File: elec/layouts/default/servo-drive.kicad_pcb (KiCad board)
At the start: 4 copper layers, 46 x 42.3 mm, 105 parts

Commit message: lots of dumb little mistaktes
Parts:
- C1, C10, C11, C12, C14, C15, C16, C18, C19, C2, C3, C33, C34, C4, C41, C43, C45, C46, C47, C5, C6, C7, C8, C9: footprint Capacitor_SMD:C_0603_1608Metric -> Capacitor_SMD:C_0402_1005Metric
- R1, R10, R11, R14, R15, R17, R18, R19, R2, R20, R21, R22, R27, R28, R3, R32, R33, R34, R35, R36, R37, R38, R39, R40, R41, R42, R43, R44, R45, R46, R7, R9: footprint Resistor_SMD:R_0603_1608Metric -> Resistor_SMD:R_0402_1005Metric
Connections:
- net servo_drive.ato:ServoDrive.power_stage.half_bridge_a.hs_fet.gate renamed servo_drive.ato:ServoDrive.power_stage.half_bridge_a.fets.gate_top
- net servo_drive.ato:ServoDrive.power_stage.half_bridge_a.ls_fet.gate renamed servo_drive.ato:ServoDrive.power_stage.half_bridge_a.fets.gate_bottom
- net servo_drive.ato:ServoDrive.power_stage.half_bridge_b.hs_fet.gate renamed servo_drive.ato:ServoDrive.power_stage.half_bridge_b.fets.gate_top
- net servo_drive.ato:ServoDrive.power_stage.half_bridge_b.ls_fet.gate renamed servo_drive.ato:ServoDrive.power_stage.half_bridge_b.fets.gate_bottom
- net servo_drive.ato:ServoDrive.power_stage.half_bridge_c.hs_fet.gate renamed servo_drive.ato:ServoDrive.power_stage.half_bridge_c.fets.gate_top
- net servo_drive.ato:ServoDrive.power_stage.half_bridge_c.ls_fet.gate renamed servo_drive.ato:ServoDrive.power_stage.half_bridge_c.fets.gate_bottom

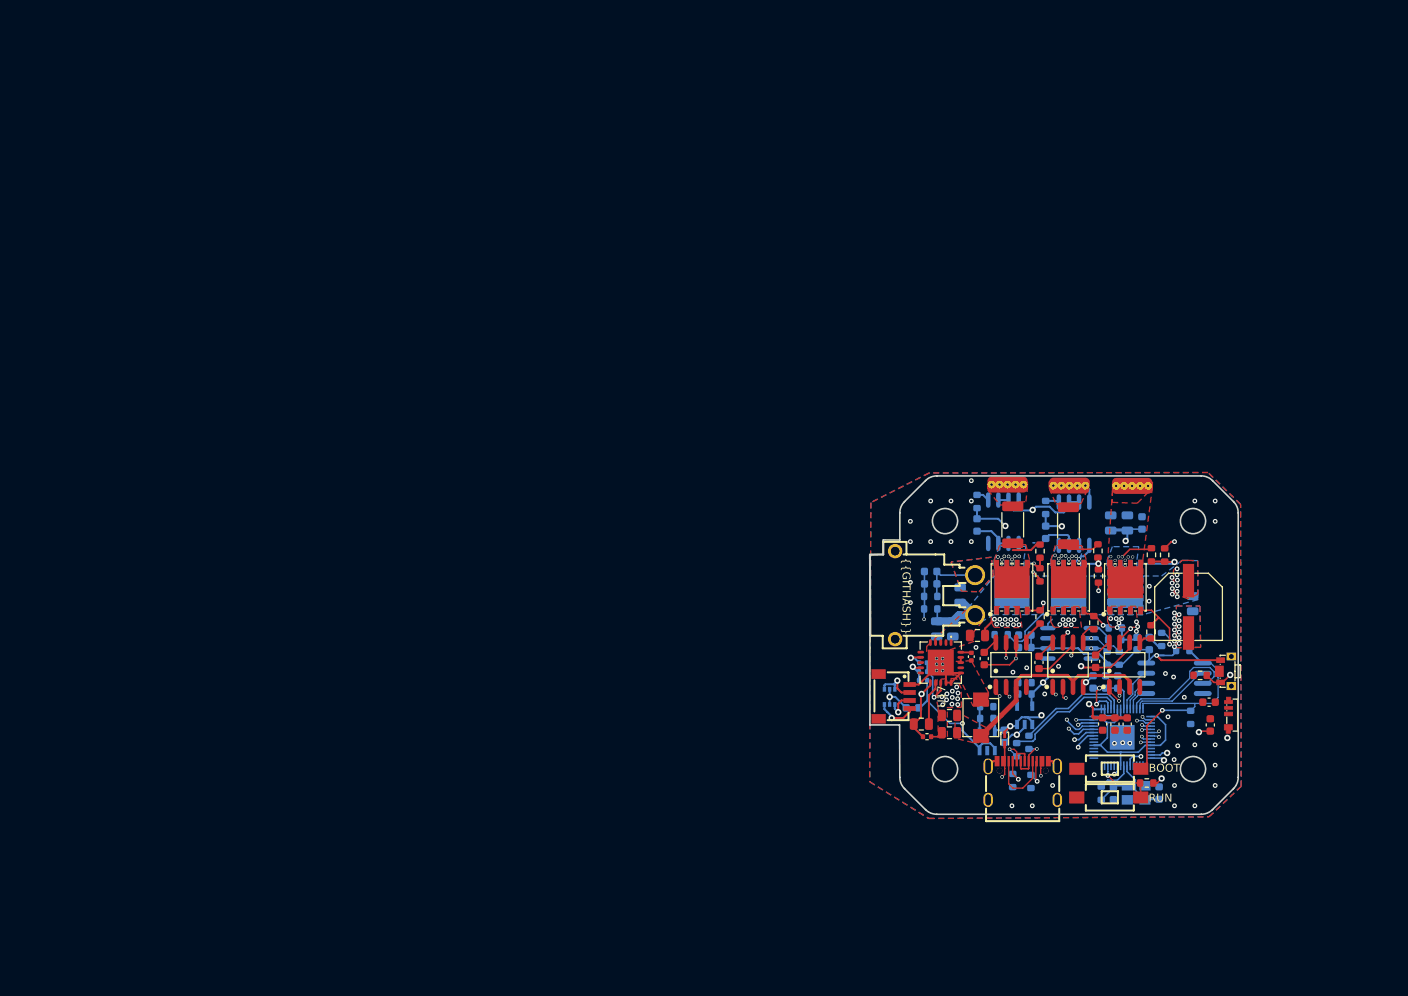
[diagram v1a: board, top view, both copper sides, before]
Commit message: mechanical outline change
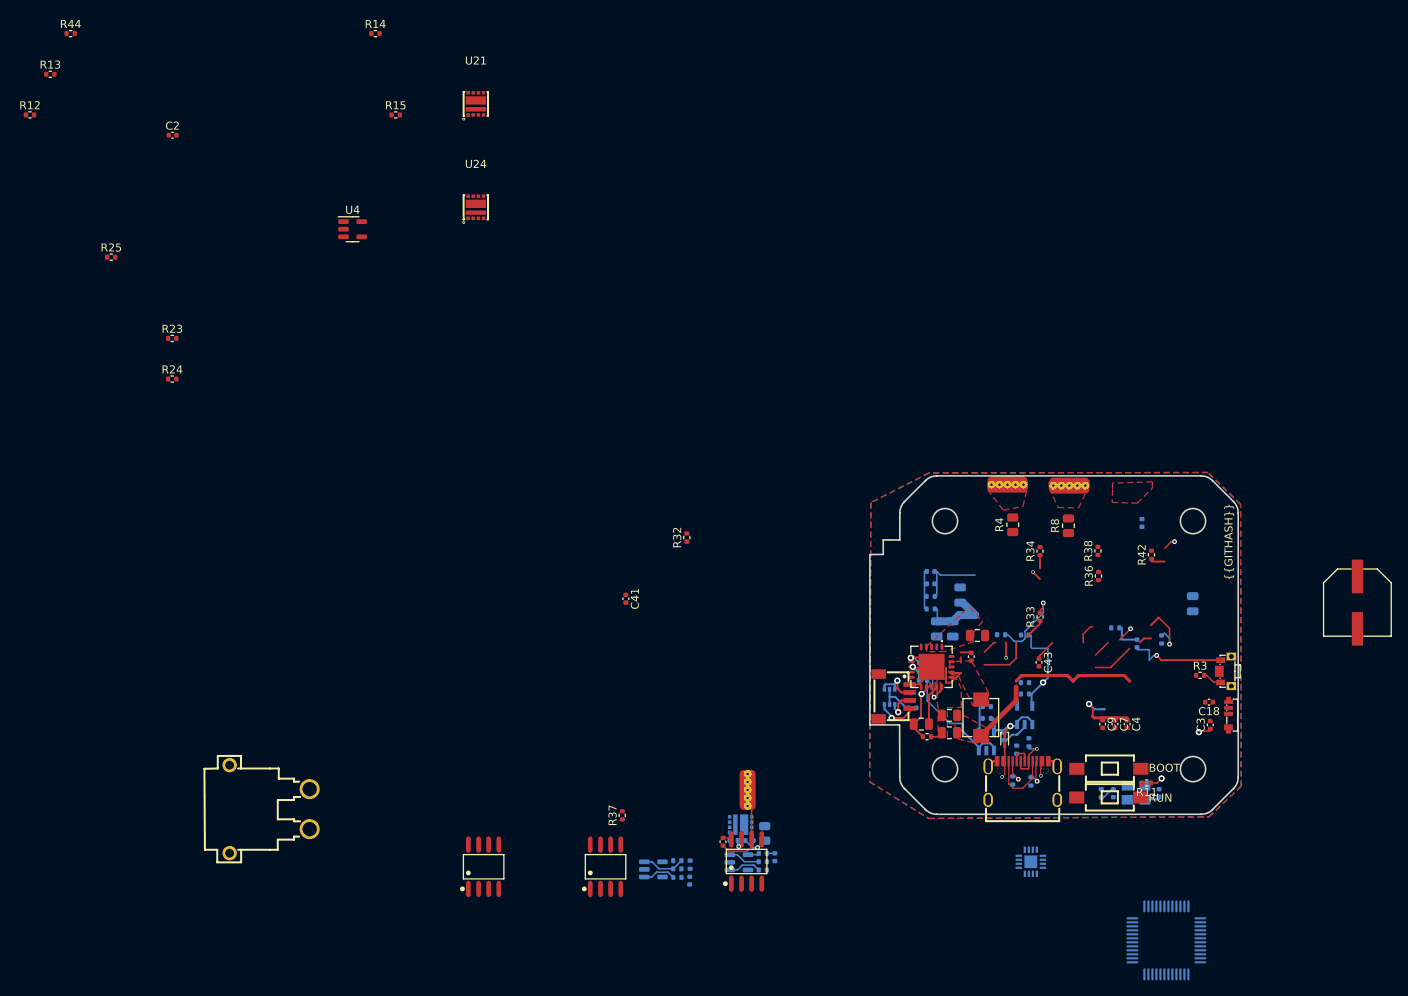
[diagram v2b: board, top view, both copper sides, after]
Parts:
- removed C10, C11, C47: 100nF, Capacitor_SMD:C_0402_1005Metric
- removed C12: 1uF, Capacitor_SMD:C_0402_1005Metric
- removed C13, C17: 1uF, Capacitor_SMD:C_0805_2012Metric
- removed Q1, Q2, Q3, Q4, Q5, Q6: , lib:DFN-8_L5.9-W5.2-P1.27-LS6.2-BL
- added R12: , Resistor_SMD:R_0402_1005Metric, F.Cu at (22.0, 33.0)
- added R13: , Resistor_SMD:R_0402_1005Metric, F.Cu at (24.6, 27.9)
- added R16: 3mOhm, Resistor_SMD:R_0805_2012Metric, B.Cu at (113.9, 122.8)
- added R23: 1k5, Resistor_SMD:R_0402_1005Metric, F.Cu at (39.8, 61.0)
- added R24: 100k, Resistor_SMD:R_0402_1005Metric, F.Cu at (39.8, 66.0)
- added R25: 100k, Resistor_SMD:R_0402_1005Metric, F.Cu at (32.2, 50.8)
- added R26: , Resistor_SMD:R_0402_1005Metric, B.Cu at (113.6, 126.4)
- added R5: 1kOhm, Resistor_SMD:R_0402_1005Metric, B.Cu at (103.0, 128.3)
- added R6: 56R, Resistor_SMD:R_0402_1005Metric, B.Cu at (104.5, 126.7)
- added U20: , Package_TO_SOT_SMD:SOT-23-5, B.Cu at (110.6, 126.4)
- added U21: , lib:V-DFN3030-8K_L3.0-W3.0-P0.65-BL, F.Cu at (77.8, 31.6)
- added U24: , lib:V-DFN3030-8K_L3.0-W3.0-P0.65-BL, F.Cu at (77.8, 44.6)
- C1, C8: value 100nF -> 2200pf
- C2: value 100nF -> 2200pf; moved to F.Cu
- R1, R2: value 100ohm -> (none)
- R11: value 1k -> 10k
- R14: value 10k -> 1kOhm; moved to F.Cu
- R15: value 1k -> 56R; moved to F.Cu
- R4, R8: footprint Resistor_SMD:R_2010_5025Metric -> Resistor_SMD:R_0805_2012Metric
- R40, R41: moved to B.Cu
- R44: value 1k -> (none); moved to F.Cu
- R45: value 10k -> 1kOhm
- R46: value 10k -> 56R
- U1: footprint lib:SOIC-8_L5.0-W4.0-P1.27-LS6.0-BL -> lib:V-DFN3030-8K_L3.0-W3.0-P0.65-BL
- U15: footprint lib:LQFN-56_L7.0-W7.0-P0.4-EP -> lib:LQFP-48_L7.0-W7.0-P0.50-LS9.0-BL
- U18: footprint lib:SOIC-8_L5.0-W4.0-P1.27-LS6.0-BL -> lib:VQFN-16_L3.0-W3.0-P0.50-BL-EP1.6
- U2: value (none) -> 8Mhz
- U3: footprint lib:SOIC-8_L5.3-W5.3-P1.27-LS8.0-BL -> Package_TO_SOT_SMD:SOT-23-5
- U4: footprint lib:SOIC-8_L5.0-W4.0-P1.27-LS6.0-BL -> Package_TO_SOT_SMD:SOT-23-5; moved to F.Cu
- moved R44 150.9 mm to (27.1, 22.9)
- moved R14 127.0 mm to (65.2, 22.9)
- moved R15 124.7 mm to (67.8, 33.0), turned to 0 degrees
- moved C2 119.9 mm to (39.9, 35.6), turned to 0 degrees
- moved U4 97.4 mm to (62.4, 47.3), turned to 0 degrees
- moved U14 87.4 mm to (52.0, 119.8)
- moved U12 70.6 mm to (78.7, 127.0)
- moved U3 69.4 mm to (100.0, 127.3), turned to 0 degrees
- moved R40 64.6 mm to (110.0, 123.7), turned to 180 degrees
- moved R2 63.8 mm to (102.9, 126.2), turned to 180 degrees
- moved R37 63.7 mm to (96.1, 120.6)
- moved U13 63.1 mm to (94.0, 127.0)
- moved U9 61.3 mm to (111.7, 117.4), turned to 0 degrees
- moved R1 59.3 mm to (102.9, 127.3), turned to 180 degrees
- moved C1 57.1 mm to (104.5, 128.7), turned to -90 degrees
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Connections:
- net servo_drive.ato:ServoDrive.micro_kit.micro.gpio12 renamed servo_drive.ato:ServoDrive.micro_kit.micro.PA5
- net servo_drive.ato:ServoDrive.micro_kit.micro.gpio16 renamed servo_drive.ato:ServoDrive.micro_kit.micro.PB14
- net servo_drive.ato:ServoDrive.micro_kit.micro.gpio17 renamed servo_drive.ato:ServoDrive.micro_kit.micro.PB15
- net servo_drive.ato:ServoDrive.micro_kit.micro.gpio22 renamed servo_drive.ato:ServoDrive.micro_kit.micro.PA13
- net servo_drive.ato:ServoDrive.micro_kit.micro.gpio28_a2 renamed servo_drive.ato:ServoDrive.micro_kit.micro.PB4
- net servo_drive.ato:ServoDrive.micro_kit.micro.gpio9 renamed servo_drive.ato:ServoDrive.power_stage.i_fb_c
- net servo_drive.ato:ServoDrive.micro_kit.micro.swdio renamed servo_drive.ato:ServoDrive.micro_kit.micro.PB12
- net servo_drive.ato:ServoDrive.position_sensor.sensor.OUT renamed servo_drive.ato:ServoDrive.position_sensor.sensor.z
- C1 pad 1: servo_drive.ato:ServoDrive.gnd -> servo_drive.ato:ServoDrive.power_stage.current_sense_a.out
- C1 pad 2: servo_drive.ato:ServoDrive.power_stage.i_fb_a -> servo_drive.ato:ServoDrive.gnd
- C14 pad 1: servo_drive.ato:ServoDrive.micro_kit.micro.xin-osc.in -> servo_drive.ato:ServoDrive.micro_kit.micro.PD0_OSC_IN-osc.in
- C2 pad 1: servo_drive.ato:ServoDrive.gnd -> servo_drive.ato:ServoDrive.power_stage.current_sense_b.out
- C2 pad 2: servo_drive.ato:ServoDrive.power_stage.i_fb_b -> servo_drive.ato:ServoDrive.gnd
- C41 pad 2: servo_drive.ato:ServoDrive.power_stage.current_sense_a.i_in-half_bridge_a.out -> servo_drive.ato:ServoDrive.power_stage.out_a
- C43 pad 2: servo_drive.ato:ServoDrive.power_stage.current_sense_b.i_in-half_bridge_b.out -> servo_drive.ato:ServoDrive.power_stage.out_b
- C8 pad 1: servo_drive.ato:ServoDrive.v_3 -> servo_drive.ato:ServoDrive.power_stage.current_sense_c.out
- R1 pad 1: servo_drive.ato:ServoDrive.power_stage.i_fb_a -> servo_drive.ato:ServoDrive.gnd
- R1 pad 2: servo_drive.ato:ServoDrive.power_stage.current_sense_a.amp.out -> servo_drive.ato:ServoDrive.power_stage.current_sense_a.feedback_div.output-opamp.in_n
- R10 pad 1: servo_drive.ato:ServoDrive.micro_kit.micro.usb_dm -> servo_drive.ato:ServoDrive.micro_kit.micro.PA11
- R11 pad 2: servo_drive.ato:ServoDrive.micro_kit.micro.run -> servo_drive.ato:ServoDrive.micro_kit.micro.NRST
- R14 pad 1: servo_drive.ato:ServoDrive.v_3 -> servo_drive.ato:ServoDrive.power_stage.current_sense_b.i_in-half_bridge_b.pwr_gnd
- R14 pad 2: servo_drive.ato:ServoDrive.micro_kit.boot_vdiv.output-flash.ncs-micro.qspi_ss_n -> servo_drive.ato:ServoDrive.power_stage.current_sense_b.opamp.in_p
- R15 pad 1: servo_drive.ato:ServoDrive.micro_kit.boot_vdiv.output-flash.ncs-micro.qspi_ss_n -> servo_drive.ato:ServoDrive.power_stage.current_sense_b.feedback_div.gnd-opamp.out-output_filter.in
- R15 pad 2: servo_drive.ato:ServoDrive.gnd -> servo_drive.ato:ServoDrive.power_stage.current_sense_b.out
- R2 pad 1: servo_drive.ato:ServoDrive.power_stage.i_fb_b -> servo_drive.ato:ServoDrive.power_stage.current_sense_a.feedback_div.output-opamp.in_n
- R2 pad 2: servo_drive.ato:ServoDrive.power_stage.current_sense_b.amp.out -> servo_drive.ato:ServoDrive.power_stage.current_sense_a.feedback_div.gnd-opamp.out-output_filter.in
- R34 pad 2: servo_drive.ato:ServoDrive.power_stage.current_sense_a.i_in-half_bridge_a.out -> servo_drive.ato:ServoDrive.power_stage.out_a
- R38 pad 2: servo_drive.ato:ServoDrive.power_stage.current_sense_b.i_in-half_bridge_b.out -> servo_drive.ato:ServoDrive.power_stage.out_b
- R4 pad 1: servo_drive.ato:ServoDrive.power_stage.current_sense_a.i_in-half_bridge_a.out -> servo_drive.ato:ServoDrive.power_stage.current_sense_a.i_in-half_bridge_a.pwr_gnd
- R4 pad 2: servo_drive.ato:ServoDrive.power_stage.out_a -> servo_drive.ato:ServoDrive.gnd
- R44 pad 1: servo_drive.ato:ServoDrive.position_sensor.sensor.PGO -> servo_drive.ato:ServoDrive.power_stage.current_sense_c.feedback_div.output-opamp.in_n
- R44 pad 2: servo_drive.ato:ServoDrive.gnd -> servo_drive.ato:ServoDrive.power_stage.current_sense_c.feedback_div.gnd-opamp.out-output_filter.in
- R45 pad 1: servo_drive.ato:ServoDrive.v_3 -> servo_drive.ato:ServoDrive.power_stage.current_sense_c.i_in-half_bridge_c.pwr_gnd
- R45 pad 2: servo_drive.ato:ServoDrive.position_sensor.sda -> servo_drive.ato:ServoDrive.power_stage.current_sense_c.opamp.in_p
- R46 pad 1: servo_drive.ato:ServoDrive.v_3 -> servo_drive.ato:ServoDrive.power_stage.current_sense_c.feedback_div.gnd-opamp.out-output_filter.in
- R46 pad 2: servo_drive.ato:ServoDrive.position_sensor.scl -> servo_drive.ato:ServoDrive.power_stage.current_sense_c.out
- R7 pad 1: servo_drive.ato:ServoDrive.micro_kit.micro.xout -> servo_drive.ato:ServoDrive.micro_kit.micro.PD1_OSC_OUT
- R8 pad 1: servo_drive.ato:ServoDrive.power_stage.current_sense_b.i_in-half_bridge_b.out -> servo_drive.ato:ServoDrive.power_stage.current_sense_b.i_in-half_bridge_b.pwr_gnd
- R8 pad 2: servo_drive.ato:ServoDrive.power_stage.out_b -> servo_drive.ato:ServoDrive.gnd
- R9 pad 1: servo_drive.ato:ServoDrive.micro_kit.micro.usb_dp -> servo_drive.ato:ServoDrive.micro_kit.micro.PA12
- S1 pad 1: servo_drive.ato:ServoDrive.micro_kit.micro.run -> servo_drive.ato:ServoDrive.micro_kit.micro.NRST
- S2 pad 1: servo_drive.ato:ServoDrive.micro_kit.boot_vdiv.output-flash.ncs-micro.qspi_ss_n -> servo_drive.ato:ServoDrive.micro_kit.micro.BOOT0
- U1 pad 1: servo_drive.ato:ServoDrive.power_stage.current_sense_a.i_in-half_bridge_a.out -> servo_drive.ato:ServoDrive.power_stage.half_bridge_c.fets.gate_top
- U1 pad 2: servo_drive.ato:ServoDrive.gnd -> servo_drive.ato:ServoDrive.vbatt
- U1 pad 3: servo_drive.ato:ServoDrive.gnd -> servo_drive.ato:ServoDrive.vbatt
- U1 pad 4: servo_drive.ato:ServoDrive.power_stage.current_sense_a.amp.NC -> servo_drive.ato:ServoDrive.vbatt
- U1 pad 5: servo_drive.ato:ServoDrive.power_stage.current_sense_a.amp.out -> servo_drive.ato:ServoDrive.power_stage.current_sense_c.i_in-half_bridge_c.pwr_gnd
- U1 pad 6: servo_drive.ato:ServoDrive.v_3 -> servo_drive.ato:ServoDrive.power_stage.current_sense_c.i_in-half_bridge_c.pwr_gnd
- U1 pad 7: servo_drive.ato:ServoDrive.v_3 -> servo_drive.ato:ServoDrive.power_stage.current_sense_c.i_in-half_bridge_c.pwr_gnd
- U1 pad 8: servo_drive.ato:ServoDrive.power_stage.out_a -> servo_drive.ato:ServoDrive.power_stage.half_bridge_c.fets.gate_bottom
- U12 pad 6: servo_drive.ato:ServoDrive.power_stage.current_sense_a.i_in-half_bridge_a.out -> servo_drive.ato:ServoDrive.power_stage.out_a
- U13 pad 6: servo_drive.ato:ServoDrive.power_stage.current_sense_b.i_in-half_bridge_b.out -> servo_drive.ato:ServoDrive.power_stage.out_b
- U15 pad 1: servo_drive.ato:ServoDrive.micro_kit.micro.iovdd -> servo_drive.ato:ServoDrive.micro_kit.micro.VBAT
- U15 pad 10: servo_drive.ato:ServoDrive.micro_kit.micro.iovdd -> servo_drive.ato:ServoDrive.power_stage.i_fb_a
- U15 pad 11: servo_drive.ato:ServoDrive.micro_kit.micro.gpio8 -> servo_drive.ato:ServoDrive.power_stage.i_fb_b
- U15 pad 13: servo_drive.ato:ServoDrive.i2c_active_terminator.bus1-stemma.sda -> servo_drive.ato:ServoDrive.voltage_input_vdiv.out
- U15 pad 14: servo_drive.ato:ServoDrive.i2c_active_terminator.bus2-stemma.scl -> servo_drive.ato:ServoDrive.micro_kit.micro.PA4
- U15 pad 16: servo_drive.ato:ServoDrive.micro_kit.micro.gpio13 -> servo_drive.ato:ServoDrive.led.data_in
- U15 pad 17: servo_drive.ato:ServoDrive.micro_kit.micro.gpio14 -> servo_drive.ato:ServoDrive.power_stage.low_in_a
- U15 pad 18: servo_drive.ato:ServoDrive.micro_kit.micro.gpio15 -> servo_drive.ato:ServoDrive.power_stage.low_in_b
- U15 pad 19: servo_drive.ato:ServoDrive.gnd -> servo_drive.ato:ServoDrive.power_stage.low_in_c
- U15 pad 2: servo_drive.ato:ServoDrive.power_stage.high_in_c -> servo_drive.ato:ServoDrive.switch.pin1
- U15 pad 20: servo_drive.ato:ServoDrive.micro_kit.micro.xin-osc.in -> servo_drive.ato:ServoDrive.micro_kit.micro.PB2
- U15 pad 21: servo_drive.ato:ServoDrive.micro_kit.micro.xout -> servo_drive.ato:ServoDrive.micro_kit.micro.PB10
- U15 pad 22: servo_drive.ato:ServoDrive.micro_kit.micro.iovdd -> servo_drive.ato:ServoDrive.micro_kit.micro.PB11
- U15 pad 23: servo_drive.ato:ServoDrive.micro_kit.micro.dvdd-micro.vreg_vout -> servo_drive.ato:ServoDrive.gnd
- U15 pad 24: servo_drive.ato:ServoDrive.micro_kit.micro.swclk -> servo_drive.ato:ServoDrive.v_3
- U15 pad 26: servo_drive.ato:ServoDrive.micro_kit.micro.run -> servo_drive.ato:ServoDrive.micro_kit.micro.PB13
- U15 pad 29: servo_drive.ato:ServoDrive.micro_kit.micro.gpio18 -> servo_drive.ato:ServoDrive.power_stage.high_in_a
- U15 pad 3: servo_drive.ato:ServoDrive.power_stage.low_in_c -> servo_drive.ato:ServoDrive.micro_kit.micro.PC14_OSC32_IN
- U15 pad 30: servo_drive.ato:ServoDrive.micro_kit.micro.gpio19 -> servo_drive.ato:ServoDrive.power_stage.high_in_b
- U15 pad 31: servo_drive.ato:ServoDrive.micro_kit.micro.gpio20 -> servo_drive.ato:ServoDrive.power_stage.high_in_c
- U15 pad 32: servo_drive.ato:ServoDrive.micro_kit.micro.gpio21 -> servo_drive.ato:ServoDrive.micro_kit.micro.PA11
- U15 pad 33: servo_drive.ato:ServoDrive.micro_kit.micro.iovdd -> servo_drive.ato:ServoDrive.micro_kit.micro.PA12
- U15 pad 35: servo_drive.ato:ServoDrive.micro_kit.micro.gpio23 -> servo_drive.ato:ServoDrive.gnd
- U15 pad 36: servo_drive.ato:ServoDrive.switch.pin1 -> servo_drive.ato:ServoDrive.v_3
- U15 pad 37: servo_drive.ato:ServoDrive.led.data_in -> servo_drive.ato:ServoDrive.micro_kit.micro.PA14
- U15 pad 38: servo_drive.ato:ServoDrive.power_stage.i_fb_a -> servo_drive.ato:ServoDrive.micro_kit.micro.PA15
- U15 pad 39: servo_drive.ato:ServoDrive.power_stage.i_fb_b -> servo_drive.ato:ServoDrive.micro_kit.micro.PB3
- U15 pad 4: servo_drive.ato:ServoDrive.power_stage.high_in_b -> servo_drive.ato:ServoDrive.micro_kit.micro.PC15_OSC32_OUT
- U15 pad 41: servo_drive.ato:ServoDrive.voltage_input_vdiv.out -> servo_drive.ato:ServoDrive.micro_kit.micro.PB5
- U15 pad 42: servo_drive.ato:ServoDrive.micro_kit.micro.iovdd -> servo_drive.ato:ServoDrive.i2c_active_terminator.bus2-stemma.scl
- U15 pad 43: servo_drive.ato:ServoDrive.v_3 -> servo_drive.ato:ServoDrive.i2c_active_terminator.bus1-stemma.sda
- U15 pad 44: servo_drive.ato:ServoDrive.v_3 -> servo_drive.ato:ServoDrive.micro_kit.micro.BOOT0
- U15 pad 45: servo_drive.ato:ServoDrive.micro_kit.micro.dvdd-micro.vreg_vout -> servo_drive.ato:ServoDrive.micro_kit.micro.PB8
- U15 pad 46: servo_drive.ato:ServoDrive.micro_kit.micro.usb_dm -> servo_drive.ato:ServoDrive.micro_kit.micro.PB9
- U15 pad 47: servo_drive.ato:ServoDrive.micro_kit.micro.usb_dp -> servo_drive.ato:ServoDrive.gnd
- U15 pad 5: servo_drive.ato:ServoDrive.power_stage.low_in_b -> servo_drive.ato:ServoDrive.micro_kit.micro.PD0_OSC_IN-osc.in
- U15 pad 6: servo_drive.ato:ServoDrive.position_sensor.sda -> servo_drive.ato:ServoDrive.micro_kit.micro.PD1_OSC_OUT
- U15 pad 7: servo_drive.ato:ServoDrive.position_sensor.scl -> servo_drive.ato:ServoDrive.micro_kit.micro.NRST
- U15 pad 8: servo_drive.ato:ServoDrive.power_stage.high_in_a -> servo_drive.ato:ServoDrive.gnd
- U15 pad 9: servo_drive.ato:ServoDrive.power_stage.low_in_a -> servo_drive.ato:ServoDrive.v_3
- U18 pad 1: servo_drive.ato:ServoDrive.v_3 -> servo_drive.ato:ServoDrive.position_sensor.sensor.ssd
- U18 pad 2: servo_drive.ato:ServoDrive.v_3 -> servo_drive.ato:ServoDrive.position_sensor.sensor.a
- U18 pad 4: servo_drive.ato:ServoDrive.gnd -> servo_drive.ato:ServoDrive.position_sensor.mosi
- U18 pad 5: servo_drive.ato:ServoDrive.position_sensor.sensor.PGO -> servo_drive.ato:ServoDrive.position_sensor.cs
- U18 pad 6: servo_drive.ato:ServoDrive.position_sensor.sda -> servo_drive.ato:ServoDrive.position_sensor.sensor.b
- U18 pad 7: servo_drive.ato:ServoDrive.position_sensor.scl -> servo_drive.ato:ServoDrive.position_sensor.miso
- U18 pad 8: servo_drive.ato:ServoDrive.position_sensor.sensor.DIR -> servo_drive.ato:ServoDrive.gnd
- U2 pad 1: servo_drive.ato:ServoDrive.micro_kit.micro.xin-osc.in -> servo_drive.ato:ServoDrive.micro_kit.micro.PD0_OSC_IN-osc.in
- U3 pad 1: servo_drive.ato:ServoDrive.micro_kit.boot_vdiv.output-flash.ncs-micro.qspi_ss_n -> servo_drive.ato:ServoDrive.power_stage.current_sense_a.opamp.in_p
- U3 pad 2: servo_drive.ato:ServoDrive.micro_kit.flash.do-micro.qspi_sd1 -> servo_drive.ato:ServoDrive.gnd
- U3 pad 3: servo_drive.ato:ServoDrive.micro_kit.flash.io2-micro.qspi_sd2 -> servo_drive.ato:ServoDrive.power_stage.current_sense_a.feedback_div.output-opamp.in_n
- U3 pad 4: servo_drive.ato:ServoDrive.gnd -> servo_drive.ato:ServoDrive.power_stage.current_sense_a.feedback_div.gnd-opamp.out-output_filter.in
- U3 pad 5: servo_drive.ato:ServoDrive.micro_kit.flash.di-micro.qspi_sd0 -> servo_drive.ato:ServoDrive.v_3
- U4 pad 1: servo_drive.ato:ServoDrive.power_stage.current_sense_b.i_in-half_bridge_b.out -> servo_drive.ato:ServoDrive.power_stage.current_sense_b.opamp.in_p
- U4 pad 3: servo_drive.ato:ServoDrive.gnd -> servo_drive.ato:ServoDrive.power_stage.current_sense_b.feedback_div.output-opamp.in_n
- U4 pad 4: servo_drive.ato:ServoDrive.power_stage.current_sense_b.amp.NC -> servo_drive.ato:ServoDrive.power_stage.current_sense_b.feedback_div.gnd-opamp.out-output_filter.in
- U4 pad 5: servo_drive.ato:ServoDrive.power_stage.current_sense_b.amp.out -> servo_drive.ato:ServoDrive.v_3
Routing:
- net servo_drive.ato:ServoDrive.v_3: track 169.8 -> 92.4 mm, vias 8 -> 6
- net servo_drive.ato:ServoDrive.power_stage.i_fb_a: track 40.5 -> 0.00 mm, vias 3 -> 0
- net servo_drive.ato:ServoDrive.i2c_active_terminator.bus1-stemma.sda: track 43.1 -> 3.80 mm, vias 2 -> 1
- net servo_drive.ato:ServoDrive.i2c_active_terminator.bus2-stemma.scl: track 44.0 -> 5.05 mm, vias 2 -> 1
- net servo_drive.ato:ServoDrive.power_stage.i_fb_b: track 34.3 -> 0.00 mm, vias 3 -> 0
- net servo_drive.ato:ServoDrive.micro_kit.boot_vdiv.output-flash.ncs-micro.qspi_ss_n: track 31.5 -> 0.00 mm, vias 1 -> 0
- net servo_drive.ato:ServoDrive.switch.pin1: track 33.2 -> 2.09 mm, vias 2 -> 0
- net servo_drive.ato:ServoDrive.v_5: track 39.3 -> 8.69 mm, vias 3 -> 1
- net servo_drive.ato:ServoDrive.power_stage.current_sense_b.i_in-half_bridge_b.out: track 28.9 -> 0.00 mm, vias 12 -> 0
- net servo_drive.ato:ServoDrive.voltage_input_vdiv.out: track 33.4 -> 4.62 mm, vias 2 -> 0
- net servo_drive.ato:ServoDrive.gnd: track 62.1 -> 34.0 mm, vias 97 -> 0
- net servo_drive.ato:ServoDrive.power_stage.current_sense_a.i_in-half_bridge_a.out: track 26.8 -> 0.00 mm, vias 10 -> 0
- net servo_drive.ato:ServoDrive.micro_kit.micro.iovdd: track 24.9 -> 0.00 mm
- net servo_drive.ato:ServoDrive.led.data_in: track 23.2 -> 0.00 mm, vias 1 -> 0
- net servo_drive.ato:ServoDrive.micro_kit.micro.dvdd-micro.vreg_vout: track 22.7 -> 0.00 mm, vias 3 -> 0
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- added copper zone on In2.Cu, net servo_drive.ato:ServoDrive.power_stage.low_in_c
- removed copper zone on B.Cu, net servo_drive.ato:ServoDrive.power_stage.current_sense_a.i_in-half_bridge_a.out
- removed copper zone on F.Cu, net servo_drive.ato:ServoDrive.power_stage.current_sense_a.i_in-half_bridge_a.out
- removed copper zone on B.Cu, net servo_drive.ato:ServoDrive.power_stage.current_sense_b.i_in-half_bridge_b.out
- removed copper zone on F.Cu, net servo_drive.ato:ServoDrive.power_stage.current_sense_b.i_in-half_bridge_b.out
- removed copper zone on B.Cu, net servo_drive.ato:ServoDrive.power_stage.out_c
- removed copper zone on B.Cu, net servo_drive.ato:ServoDrive.vbatt

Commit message: layout progress
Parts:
- removed C39: 100uF, lib:CAP-SMD_BD8.0-L8.3-W8.3-FD
- added U17: , lib:CONN-SMD_4P-P1.00_SM04B-SRSS-TB-LF-SN, B.Cu at (210.9, 119.1)
- C26, C31, C32, C4, C7, C9, J1, R23, U11, U14, U5: moved to B.Cu
- C28, C29, C30, R16, R29, R30, R35, U1: moved to F.Cu
- moved U14 182.1 mm to (233.9, 112.7), turned to 180 degrees
- moved U21 181.8 mm to (250.8, 87.5), turned to -90 degrees
- moved R23 181.4 mm to (217.9, 95.4), turned to -45 degrees
- moved C2 169.4 mm to (177.3, 134.6)
- moved C45 169.0 mm to (276.6, 105.6), turned to 180 degrees
- moved R40 167.6 mm to (276.8, 106.9), turned to 90 degrees
- moved R41 165.5 mm to (276.8, 108.9), turned to -90 degrees
- moved U20 164.5 mm to (274.1, 107.5), turned to -90 degrees
- moved R46 162.2 mm to (275.2, 110.5), turned to -90 degrees
- moved R26 161.3 mm to (274.1, 110.5), turned to 90 degrees
- moved U3 160.7 mm to (254.2, 82.1), turned to 180 degrees
- moved R45 160.3 mm to (273.1, 110.5), turned to 90 degrees
- moved C8 160.1 mm to (274.7, 112.0), turned to 180 degrees
- moved U24 159.6 mm to (228.9, 95.8), turned to -90 degrees
- moved R5 155.5 mm to (251.2, 81.1), turned to 0 degrees
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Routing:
- net servo_drive.ato:ServoDrive.v_3: track 92.4 -> 1.47 mm, vias 6 -> 1
- net servo_drive.ato:ServoDrive.v_10: track 38.4 -> 2.82 mm
- net servo_drive.ato:ServoDrive.gnd: track 34.0 -> 6.12 mm
- net servo_drive.ato:ServoDrive.power_stage.half_bridge_c.gate_driver.hvg: track 18.7 -> 0.00 mm, vias 3 -> 0
- net servo_drive.ato:ServoDrive.power_stage.half_bridge_a.gate_driver.hvg: track 15.4 -> 0.00 mm, vias 2 -> 0
- net servo_drive.ato:ServoDrive.buck.SGND: track 16.0 -> 0.92 mm, vias 2 -> 0
- net servo_drive.ato:ServoDrive.power_stage.out_c: track 14.7 -> 0.00 mm
- net servo_drive.ato:ServoDrive.usb.vbus-usb_diode.anode: track 11.1 -> 0.00 mm, vias 2 -> 0
- net servo_drive.ato:ServoDrive.power_stage.half_bridge_a.fets.gate_bottom: track 9.12 -> 0.00 mm, vias 1 -> 0
- net servo_drive.ato:ServoDrive.usb.sbu: track 8.69 -> 0.00 mm
- net servo_drive.ato:ServoDrive.power_stage.half_bridge_c.fets.gate_bottom: track 8.06 -> 0.00 mm, vias 1 -> 0
- net servo_drive.ato:ServoDrive.v_5: track 8.69 -> 2.17 mm, vias 1 -> 0
- net servo_drive.ato:ServoDrive.power_stage.out_a: track 6.29 -> 0.00 mm
- net servo_drive.ato:ServoDrive.micro_kit.usb_dp-usb.dp: track 5.91 -> 0.00 mm, vias 1 -> 0
- net servo_drive.ato:ServoDrive.buck.buck_converter.VCC: track 5.49 -> 0.00 mm
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- removed copper zone on F.Cu, net servo_drive.ato:ServoDrive.buck.buck_converter.LX
- removed copper zone on B.Cu, net servo_drive.ato:ServoDrive.gnd
- removed copper zone on F.Cu, net servo_drive.ato:ServoDrive.gnd
- removed copper zone on In1.Cu, net servo_drive.ato:ServoDrive.gnd
- removed copper zone on In2.Cu, net servo_drive.ato:ServoDrive.gnd
- removed copper zone on In2.Cu, net servo_drive.ato:ServoDrive.power_stage.low_in_c
- removed copper zone on F.Cu, net servo_drive.ato:ServoDrive.power_stage.out_a
- removed copper zone on F.Cu, net servo_drive.ato:ServoDrive.power_stage.out_b
- removed copper zone on F.Cu, net servo_drive.ato:ServoDrive.power_stage.out_c
- removed copper zone on F.Cu, net servo_drive.ato:ServoDrive.v_10
- removed copper zone on In1.Cu, net servo_drive.ato:ServoDrive.v_3
- removed copper zone on F.Cu, net servo_drive.ato:ServoDrive.vbatt
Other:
- board size 46 x 42.3 mm -> 37.5 x 39.9 mm
- board text removed: "BOOT"
- board text removed: "RUN"

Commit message: sync layout with ato src
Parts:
- removed the U17 at (210.9, 119.1)
- added C1: 1uF, Capacitor_SMD:C_0402_1005Metric, F.Cu at (170.1, 124.2)
- added C13: 100nF, Capacitor_SMD:C_0402_1005Metric, F.Cu at (159.8, 143.3)
- added C17: 10nF, Capacitor_SMD:C_0402_1005Metric, F.Cu at (159.8, 145.3)
- added C2: 1uF, Capacitor_SMD:C_0402_1005Metric, F.Cu at (145.6, 147.6)
- added C20: 10uF, Capacitor_SMD:C_1206_3216Metric, F.Cu at (147.0, 124.9)
- added C21: 10uF, Capacitor_SMD:C_1206_3216Metric, F.Cu at (147.0, 128.3)
- added C22: 10uF, Capacitor_SMD:C_1206_3216Metric, F.Cu at (147.0, 131.6)
- added C39: 10uF, Capacitor_SMD:C_1206_3216Metric, F.Cu at (147.0, 135.0)
- added C8: , Capacitor_SMD:C_0402_1005Metric, F.Cu at (167.7, 139.3)
- added R1: 10kOhm, Resistor_SMD:R_0402_1005Metric, F.Cu at (145.7, 145.6)
- added R13: , Resistor_SMD:R_0402_1005Metric, F.Cu at (145.7, 139.6)
- added R2: 10kOhm, Resistor_SMD:R_0402_1005Metric, F.Cu at (164.8, 139.3)
- added R44: , Resistor_SMD:R_0402_1005Metric, F.Cu at (164.8, 145.3)
- added R50: , Resistor_SMD:R_0402_1005Metric, F.Cu at (169.7, 145.3)
- added R51: , Resistor_SMD:R_0402_1005Metric, F.Cu at (169.7, 147.3)
- added R53: 60R, Resistor_SMD:R_0402_1005Metric, F.Cu at (159.8, 139.3)
- added R54: 60R, Resistor_SMD:R_0402_1005Metric, F.Cu at (159.8, 141.3)
- added U25: , lib:SOIC-8_L4.9-W3.9-P1.27-LS6.0-BL, F.Cu at (155.3, 142.7)
- added U26: , lib:CONN-SMD_4P-P1.00_SM04B-SRSS-TB-LF-SN, F.Cu at (155.7, 126.5)
- added U27: , lib:CONN-SMD_4P-P1.00_SM04B-SRSS-TB-LF-SN, F.Cu at (155.7, 133.0)
- added U4: , lib:SOIC-8_L5.0-W4.0-P1.27-LS6.0-BL, F.Cu at (165.5, 127.4)
- C28, D1, R3: moved to B.Cu
- C5, R17, R18, R19, R20, R21, R22, R39, R40, R41, R43, U22, U23: moved to F.Cu
- R14: value 1kOhm -> (none)
- R45: value 1kOhm -> (none); moved to F.Cu
- R49: renamed from R44; moved to B.Cu
- R5: value 1kOhm -> 10kOhm; moved to F.Cu
- moved R37 136.6 mm to (230.6, 97.0), turned to 0 degrees
- moved C41 132.2 mm to (228.5, 86.4), turned to 180 degrees
- moved R49 116.9 mm to (251.3, 107.6), turned to -90 degrees
- moved R45 114.4 mm to (164.8, 147.3), turned to 0 degrees
- moved R5 105.3 mm to (164.8, 141.3)
- moved C44 95.5 mm to (233.7, 98.3), turned to 0 degrees
- moved C40 93.5 mm to (233.7, 105.9)
- moved R27 88.1 mm to (221.0, 77.2)
- moved R28 88.0 mm to (221.0, 76.2)
- moved C33 87.9 mm to (221.0, 75.2)
- moved C34 87.8 mm to (221.0, 74.3)
- moved R19 76.5 mm to (221.0, 116.2)
- moved R38 75.5 mm to (230.6, 95.4), turned to 180 degrees
- moved R36 75.1 mm to (230.6, 93.3), turned to 0 degrees
- moved R39 73.0 mm to (230.6, 98.1), turned to 180 degrees
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- renumbered C1 to C10, C2 to C11, C8 to C12, R2 to R12, R23 to R15, R6 to R16, R24 to R23, R25 to R24, R12 to R25, R13 to R26, R15 to R46, R16 to R47, R26 to R48, R46 to R52, R1 to R6, U24 to U1, U3 to U20, U4 to U21, U20 to U24, U21 to U28, U1 to U3
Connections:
- R14 pad 1: servo_drive.ato:ServoDrive.power_stage.current_sense_b.i_in-half_bridge_b.pwr_gnd -> servo_drive.ato:ServoDrive.power_stage.current_sense_a.bias_div.output-opamp.in_p
- R14 pad 2: servo_drive.ato:ServoDrive.power_stage.current_sense_b.opamp.in_p -> servo_drive.ato:ServoDrive.v_3
- R45 pad 1: servo_drive.ato:ServoDrive.power_stage.current_sense_c.i_in-half_bridge_c.pwr_gnd -> servo_drive.ato:ServoDrive.power_stage.current_sense_b.bias_div.output-opamp.in_p
- R45 pad 2: servo_drive.ato:ServoDrive.power_stage.current_sense_c.opamp.in_p -> servo_drive.ato:ServoDrive.v_3
- R5 pad 1: servo_drive.ato:ServoDrive.power_stage.current_sense_a.i_in-half_bridge_a.pwr_gnd -> servo_drive.ato:ServoDrive.power_stage.reference.buffer.in_p_b-half_ref.output
- R5 pad 2: servo_drive.ato:ServoDrive.power_stage.current_sense_a.opamp.in_p -> servo_drive.ato:ServoDrive.gnd
- U15 pad 45: servo_drive.ato:ServoDrive.micro_kit.micro.PB8 -> servo_drive.ato:ServoDrive.canbus.can_rx
- U15 pad 46: servo_drive.ato:ServoDrive.micro_kit.micro.PB9 -> servo_drive.ato:ServoDrive.canbus.can_tx
- U20 pad 1: servo_drive.ato:ServoDrive.power_stage.current_sense_a.opamp.in_p -> servo_drive.ato:ServoDrive.power_stage.current_sense_a.bias_div.output-opamp.in_p
- U21 pad 1: servo_drive.ato:ServoDrive.power_stage.current_sense_b.opamp.in_p -> servo_drive.ato:ServoDrive.power_stage.current_sense_b.bias_div.output-opamp.in_p
- U24 pad 1: servo_drive.ato:ServoDrive.power_stage.current_sense_c.opamp.in_p -> servo_drive.ato:ServoDrive.power_stage.current_sense_c.bias_div.output-opamp.in_p
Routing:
- net servo_drive.ato:ServoDrive.gnd: track 6.12 -> 30.9 mm, vias 0 -> 38
- net servo_drive.ato:ServoDrive.power_stage.out_a: track 0.00 -> 11.2 mm
- net servo_drive.ato:ServoDrive.power_stage.out_c: track 0.00 -> 11.2 mm
- net servo_drive.ato:ServoDrive.power_stage.out_b: track 0.00 -> 11.2 mm
- net servo_drive.ato:ServoDrive.power_stage.current_sense_a.i_in-half_bridge_a.pwr_gnd: track 0.00 -> 9.10 mm, vias 0 -> 2
- net servo_drive.ato:ServoDrive.power_stage.half_bridge_c.fets.gate_top: track 0.00 -> 9.04 mm, vias 0 -> 2
- net servo_drive.ato:ServoDrive.power_stage.half_bridge_b.fets.gate_top: track 0.00 -> 8.84 mm, vias 0 -> 2
- net servo_drive.ato:ServoDrive.power_stage.half_bridge_a.fets.gate_top: track 0.00 -> 7.65 mm, vias 0 -> 2
- net servo_drive.ato:ServoDrive.power_stage.half_bridge_b.fets.gate_bottom: track 0.00 -> 6.64 mm, vias 0 -> 2
- net servo_drive.ato:ServoDrive.power_stage.half_bridge_c.fets.gate_bottom: track 0.00 -> 6.58 mm, vias 0 -> 2
- net servo_drive.ato:ServoDrive.power_stage.half_bridge_a.fets.gate_bottom: track 0.00 -> 5.67 mm, vias 0 -> 2
- net servo_drive.ato:ServoDrive.v_5: track 2.17 -> 7.50 mm
- net servo_drive.ato:ServoDrive.power_stage.current_sense_a.feedback_div.gnd-opamp.out-output_filter.in: track 0.00 -> 4.72 mm
- net servo_drive.ato:ServoDrive.voltage_input_vdiv.out: track 4.62 -> 0.00 mm
- net servo_drive.ato:ServoDrive.buck.SGND: track 0.92 -> 5.24 mm
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- added copper zone on B.Cu, net servo_drive.ato:ServoDrive.gnd
- added copper zone on F.Cu, net servo_drive.ato:ServoDrive.gnd
- added copper zone on In2.Cu, net servo_drive.ato:ServoDrive.gnd
- added copper zone on F.Cu, net servo_drive.ato:ServoDrive.power_stage.current_sense_a.i_in-half_bridge_a.pwr_gnd
- added copper zone on F.Cu, net servo_drive.ato:ServoDrive.power_stage.current_sense_b.i_in-half_bridge_b.pwr_gnd
- added copper zone on F.Cu, net servo_drive.ato:ServoDrive.power_stage.current_sense_c.i_in-half_bridge_c.pwr_gnd
- added copper zone on B.Cu, net servo_drive.ato:ServoDrive.vbatt
- added copper zone on F.Cu, net servo_drive.ato:ServoDrive.vbatt
- added copper zone on In2.Cu, net servo_drive.ato:ServoDrive.vbatt
